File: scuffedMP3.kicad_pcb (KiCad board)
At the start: 2 copper layers, 24 x 16 mm, 10 parts, among them J1 OLED, J2 Micro_SD_Card, J3 AudioJack3, U1 ESP32-WROVER-E, U2 TP4056-42-ESOP8, U3 CP2102N-Axx-xQFN24, U4 MCP1825S, U5 PCM5102A

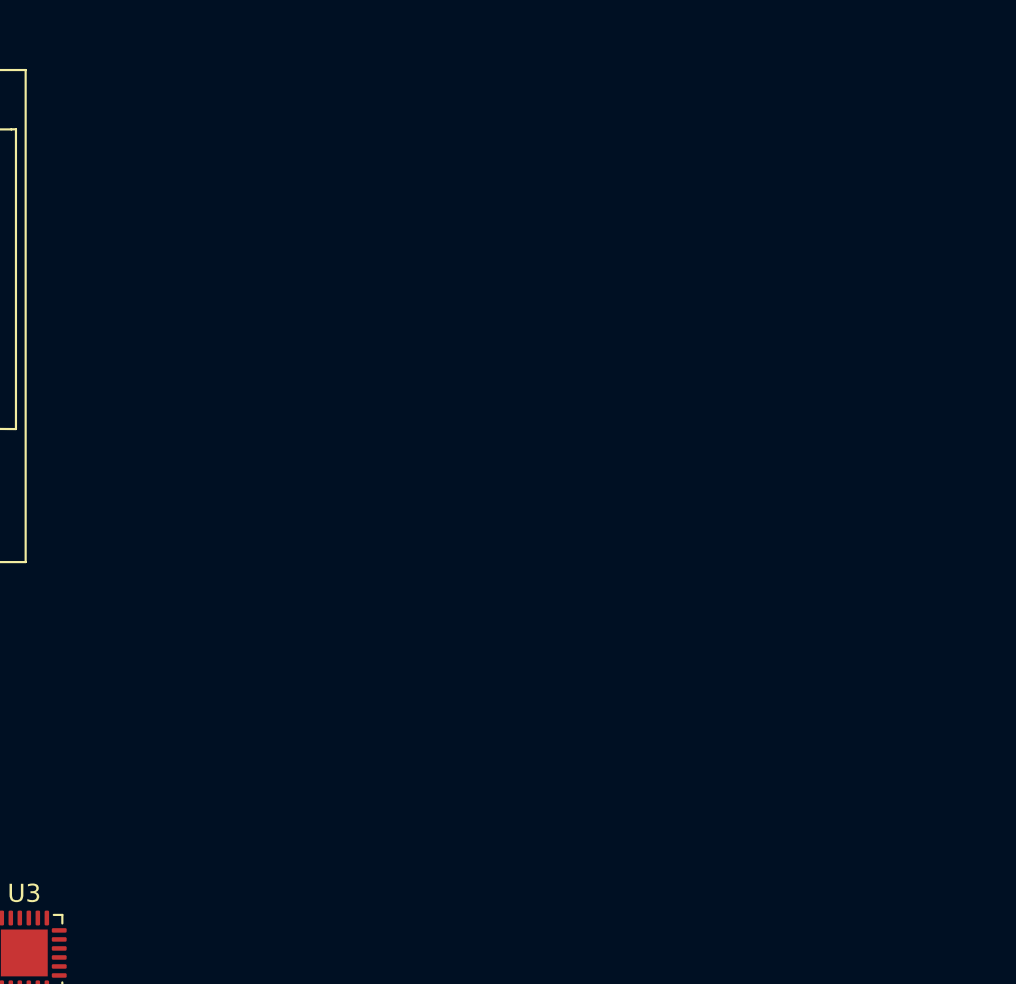
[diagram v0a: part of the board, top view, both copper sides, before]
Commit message: add touch sensor and wheel
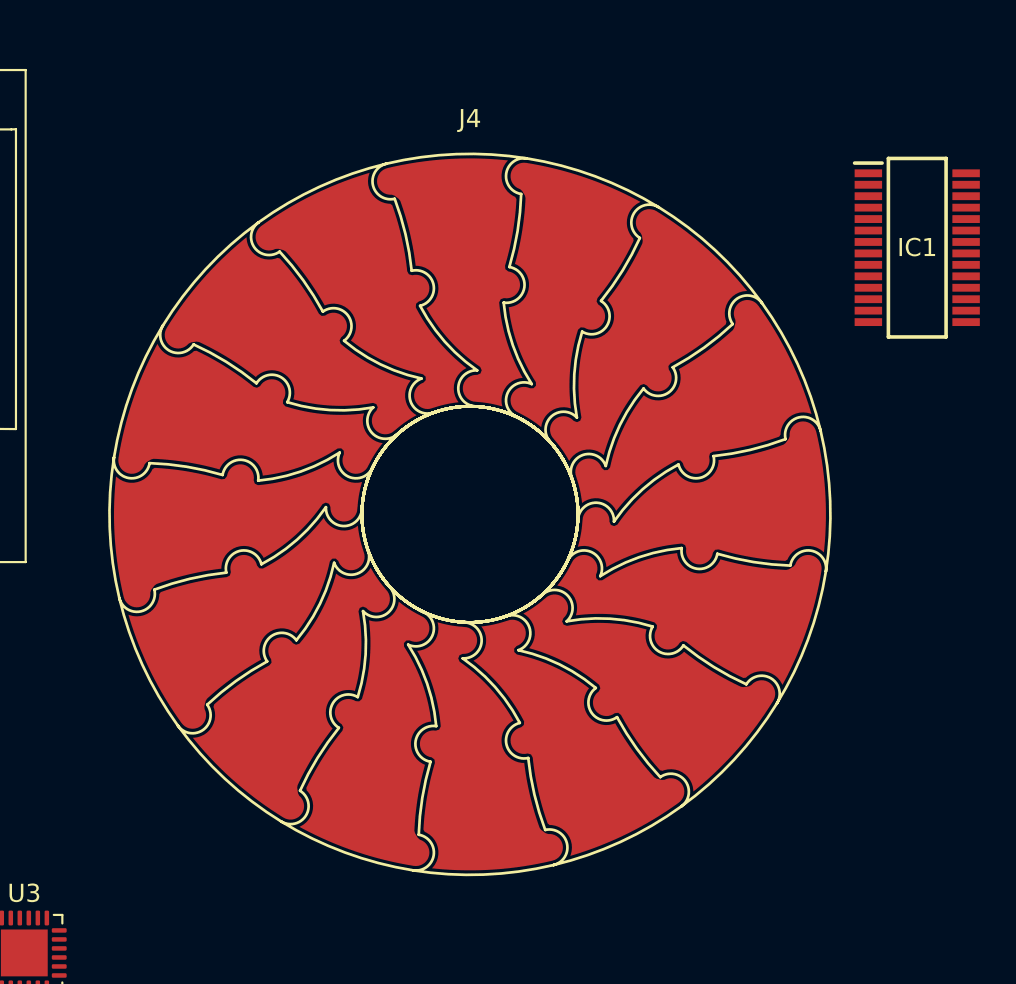
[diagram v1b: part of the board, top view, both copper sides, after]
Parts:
- added IC1: TTP229-BSF, TTP229-BSF:SOP64P600X175-28N, F.Cu at (131.3, 39.9)
- added J4: Conn_01x16_Pin, Library:ScrollWheel-40x12mm, F.Cu at (106.5, 54.7)
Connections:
- U1 pad 6: unconnected-(U1-GPIO34/ADC1_CH6-Pad6) -> Net-(IC1-SCL)
- U1 pad 7: unconnected-(U1-GPIO35/ADC1_CH7-Pad7) -> Net-(IC1-SDO)

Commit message: upd
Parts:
- removed BT1: Battery, Connector_JST:JST_PH_S2B-PH-K_1x02_P2.00mm_Horizontal
- added 10kΩ1: R, Resistor_SMD:R_0603_1608Metric, F.Cu at (108.4, 81.6)
- added C1: 1 µF, Capacitor_SMD:C_0603_1608Metric, F.Cu at (108.4, 84.1)
- added C10: 1 µF, Capacitor_SMD:C_0603_1608Metric, F.Cu at (112.4, 89.1)
- added C11: 0.1uF, Capacitor_SMD:C_0603_1608Metric, F.Cu at (112.4, 91.7)
- added C12: 0.1 µF, Capacitor_SMD:C_0603_1608Metric, F.Cu at (112.4, 94.2)
- added C13: 0.1 µF, Capacitor_SMD:C_0603_1608Metric, F.Cu at (112.4, 96.7)
- added C14: 1 µF, Capacitor_SMD:C_0603_1608Metric, F.Cu at (116.4, 81.6)
- added C15: 1 µF, Capacitor_SMD:C_0603_1608Metric, F.Cu at (116.4, 84.1)
- added C16: 1 µF, Capacitor_SMD:C_0603_1608Metric, F.Cu at (116.4, 86.6)
- added C17: 0.1 µF, Capacitor_SMD:C_0603_1608Metric, F.Cu at (116.4, 89.1)
- added C18: 0.1 µF, Capacitor_SMD:C_0603_1608Metric, F.Cu at (116.4, 91.7)
- added C2: 0.1 µF, Capacitor_SMD:C_0603_1608Metric, F.Cu at (108.4, 86.6)
- added C3: 1 µF, Capacitor_SMD:C_0603_1608Metric, F.Cu at (108.4, 89.1)
- added C4: 0.1 µF, Capacitor_SMD:C_0603_1608Metric, F.Cu at (108.4, 91.7)
- added C5: 0.1µF, Capacitor_SMD:C_0603_1608Metric, F.Cu at (108.4, 94.2)
- added C6: 0.1µF, Capacitor_SMD:C_0603_1608Metric, F.Cu at (108.4, 96.7)
- added C7: 0.1µF, Capacitor_SMD:C_0603_1608Metric, F.Cu at (112.4, 81.6)
- added C8: 1 µF, Capacitor_SMD:C_0603_1608Metric, F.Cu at (112.4, 84.1)
- added C9: 1 µF, Capacitor_SMD:C_0603_1608Metric, F.Cu at (112.4, 86.6)
- added R1: 10kΩ, Resistor_SMD:R_0603_1608Metric, F.Cu at (116.4, 94.2)
- added R2: 1.2 kΩ, Resistor_SMD:R_0603_1608Metric, F.Cu at (116.4, 96.7)
- added R3: 10 kΩ, Resistor_SMD:R_0603_1608Metric, F.Cu at (120.4, 81.6)
- added R4: 10 kΩ, Resistor_SMD:R_0603_1608Metric, F.Cu at (120.4, 84.1)
- added R5: 5.1 kΩ, Resistor_SMD:R_0603_1608Metric, F.Cu at (120.4, 86.6)
- added R6: 5.1 kΩ, Resistor_SMD:R_0603_1608Metric, F.Cu at (120.4, 89.1)
- added SW1: SW_SPST, Button_Switch_SMD:SW_DIP_SPSTx01_Slide_6.7x4.1mm_W6.73mm_P2.54mm_LowProfile_JPin, F.Cu at (165.2, 113.4)
- added U6: HS24S010B, OLED:LCD-TH_L72.3-W43.0_HS24S010B, F.Cu at (199.2, 40.3)
- J1: value OLED -> battery; footprint OLED:128x64OLED -> PHR-2:JST_PHR-2
- J2: value Micro_SD_Card -> DM3AT-SF-PEJM5; footprint Connector_Card:SD_Card_Device_16mm_SlotDepth -> micro_sd:HRS_DM3AT-SF-PEJM5
- J4: footprint Library:ScrollWheel-40x12mm -> Wheel:ScrollWheel-60x35mm
- moved U5 190.8 mm to (223.1, 123.9)
- moved J3 184.6 mm to (231.8, 129.5), turned to 90 degrees
- moved J2 164.2 mm to (230.9, 70.0), turned to 90 degrees
- moved U1 163.7 mm to (199.8, 94.3)
- moved J1 142.9 mm to (187.0, 121.3), turned to 90 degrees
- moved U4 140.0 mm to (176.1, 125.0)
- moved USB1 138.1 mm to (165.3, 128.6)
- moved J4 101.4 mm to (198.9, 96.5)
- moved U3 99.3 mm to (173.0, 118.0)
- moved U2 93.8 mm to (164.6, 105.1)
- moved IC1 48.8 mm to (167.7, 72.3)
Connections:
- net Net-(IC1-TP0) renamed /TOUCH TP0
- net Net-(IC1-TP1) renamed /TOUCH TP1
- net Net-(IC1-TP2) renamed /TOUCH TP2
- net Net-(IC1-TP3) renamed /TOUCH TP3
- net Net-(IC1-TP4) renamed /TOUCH TP4
- IC1 pad 10: Net-(IC1-TP13) -> /TOUCH TP13
- IC1 pad 11: Net-(IC1-TP12) -> /TOUCH TP12
- IC1 pad 12: Net-(IC1-SDO) -> /TOUCH SDO
- IC1 pad 13: Net-(IC1-SCL) -> /TOUCH SCL
- IC1 pad 14: unconnected-(IC1-SLPSENB-Pad14) -> GND
- IC1 pad 15: Net-(IC1-TP11) -> /TOUCH TP11
- IC1 pad 16: Net-(IC1-TP10) -> /TOUCH TP10
- IC1 pad 17: unconnected-(IC1-SENADJ2-Pad17) -> GND
- IC1 pad 18: Net-(IC1-TP9) -> /TOUCH TP9
- IC1 pad 19: Net-(IC1-TP8) -> /TOUCH TP8
- IC1 pad 20: unconnected-(IC1-TEST-Pad20) -> GND
- IC1 pad 21: Net-(IC1-TP7) -> /TOUCH TP7
- IC1 pad 22: Net-(IC1-TP6) -> /TOUCH TP6
- IC1 pad 23: unconnected-(IC1-SENADJ1-Pad23) -> GND
- IC1 pad 24: Net-(IC1-TP5) -> /TOUCH TP5
- IC1 pad 26: Net-(IC1-VDD) -> +3V3
- IC1 pad 27: Net-(BT1--) -> GND
- IC1 pad 28: unconnected-(IC1-SLPSENA-Pad28) -> Net-(IC1-SLPSENA)
- IC1 pad 4: unconnected-(IC1-SENADJ0-Pad4) -> GND
- IC1 pad 7: Net-(IC1-TP15) -> /TOUCH TP15
- IC1 pad 8: Net-(IC1-TP14) -> /TOUCH TP14
- IC1 pad 9: unconnected-(IC1-SENADJ3-Pad9) -> +3V3
- J1 pad 1: Net-(J1-Pin_1) -> /BAT
- J1 pad 2: Net-(J1-Pin_2) -> GND
- J2 pad 2: Net-(J2-DAT3/CD) -> /MICRO CD
- J2 pad 3: Net-(J2-CMD) -> /MICRO CMD
- J2 pad 4: Net-(IC1-VDD) -> +3V3
- J2 pad 5: Net-(J2-CLK) -> /MICRO CLK
- J2 pad 6: Net-(BT1--) -> GND
- J2 pad 7: Net-(J2-DAT0) -> /MICRO DAT0
- J3 pad S: Net-(BT1--) -> GND
- U1 pad 1: Net-(BT1--) -> GND
- U1 pad 10: Net-(U1-DAC_1/ADC2_CH8/GPIO25) -> /LR CLOCK
- U1 pad 11: Net-(U1-DAC_2/ADC2_CH9/GPIO26) -> /Bit Clock
- U1 pad 12: Net-(U1-ADC2_CH7/GPIO27) -> /OLED DC
- U1 pad 15: Net-(BT1--) -> GND
- U1 pad 2: Net-(IC1-VDD) -> +3V3
- U1 pad 24: unconnected-(U1-ADC2_CH2/GPIO2-Pad24) -> /MICRO CLK
- U1 pad 25: unconnected-(U1-GPIO0/BOOT/ADC2_CH1-Pad25) -> /BOOT_SEL
- U1 pad 26: unconnected-(U1-ADC2_CH0/GPIO4-Pad26) -> /MICRO CMD
- U1 pad 29: Net-(J2-DAT3/CD) -> /OLED CS
- U1 pad 3: unconnected-(U1-EN/CHIP_PU-Pad3) -> /EN
- U1 pad 30: Net-(J2-CLK) -> /OLED SCL
- U1 pad 31: Net-(J2-DAT0) -> /OLED RST
- U1 pad 33: Net-(J1-Pin_1) -> /OLED LED
- U1 pad 34: Net-(U1-U0RXD/GPIO3) -> /UART_RXD
- U1 pad 35: Net-(U1-U0TXD/GPIO1) -> /UART_TXD
- U1 pad 36: Net-(J1-Pin_2) -> /DAC DIN
- U1 pad 37: Net-(J2-CMD) -> /MOSI OLED
- U1 pad 38: Net-(BT1--) -> GND
- U1 pad 6: Net-(IC1-SCL) -> unconnected-(U1-GPIO34/ADC1_CH6-Pad6)
- U1 pad 7: Net-(IC1-SDO) -> unconnected-(U1-GPIO35/ADC1_CH7-Pad7)
- U1 pad 8: unconnected-(U1-32K_XP/GPIO32/ADC1_CH4-Pad8) -> /MICRO DAT0
- U1 pad 9: unconnected-(U1-32K_XN/GPIO33/ADC1_CH5-Pad9) -> /TOUCH SCL
- U2 pad 2: unconnected-(U2-PROG-Pad2) -> Net-(U2-PROG)
- U2 pad 3: Net-(BT1--) -> GND
- U2 pad 4: Net-(U2-V_{CC}) -> VBUS
- U2 pad 5: Net-(BT1-+) -> /BAT
- U2 pad 8: Net-(BT1--) -> VBUS
- U3 pad 19: unconnected-(U3-~{RTS}-Pad19) -> Net-(U3-~{RTS})
- U3 pad 2: Net-(BT1--) -> GND
- U3 pad 20: Net-(U1-U0TXD/GPIO1) -> /UART_RXD
- U3 pad 21: Net-(U1-U0RXD/GPIO3) -> /UART_TXD
- U3 pad 23: unconnected-(U3-~{DTR}-Pad23) -> Net-(U3-~{DTR})
- U3 pad 25: Net-(BT1--) -> GND
- U3 pad 3: unconnected-(U3-D+-Pad3) -> /USB_DP
- U3 pad 4: unconnected-(U3-D--Pad4) -> /USB_DM
- U3 pad 6: unconnected-(U3-VDD-Pad6) -> +3V3
- U3 pad 7: unconnected-(U3-VREGIN-Pad7) -> VBUS
- U3 pad 8: unconnected-(U3-VBUS-Pad8) -> VBUS
- U3 pad 9: unconnected-(U3-~{RST}-Pad9) -> Net-(U3-~{RST})
- U4 pad 1: Net-(BT1-+) -> VBUS
- U4 pad 2: Net-(BT1--) -> GND
- U4 pad 3: Net-(IC1-VDD) -> /3V3 IN
- U5 pad 1: Net-(IC1-VDD) -> +3V3
- U5 pad 10: Net-(BT1--) -> unconnected-(U5-DEMP-Pad10)
- U5 pad 11: Net-(BT1--) -> unconnected-(U5-FLT-Pad11)
- U5 pad 13: Net-(U1-ADC2_CH7/GPIO27) -> /Bit Clock
- U5 pad 14: Net-(U1-DAC_1/ADC2_CH8/GPIO25) -> /DAC DIN
- U5 pad 15: Net-(U1-DAC_2/ADC2_CH9/GPIO26) -> /LR CLOCK
- U5 pad 16: Net-(BT1--) -> GND
- U5 pad 17: Net-(IC1-VDD) -> GND
- U5 pad 19: Net-(BT1--) -> GND
- U5 pad 2: unconnected-(U5-CAPP-Pad2) -> Net-(U5-CAPP)
- U5 pad 20: Net-(IC1-VDD) -> +3V3
- U5 pad 3: Net-(BT1--) -> GND
- U5 pad 4: unconnected-(U5-CAPM-Pad4) -> Net-(U5-CAPM)
- U5 pad 5: Net-(BT1--) -> Net-(U5-VNEG)
- U5 pad 8: Net-(IC1-VDD) -> +3V3
- U5 pad 9: Net-(BT1--) -> GND
- USB1 pad 1: unconnected-(USB1-GND-Pad1) -> GND
- USB1 pad 12: unconnected-(USB1-GND-Pad12) -> GND
- USB1 pad 13: unconnected-(USB1-GND-Pad13) -> GND
- USB1 pad 16: unconnected-(USB1-VBUS-Pad16) -> VBUS
- USB1 pad 17: unconnected-(USB1-CC2-Pad17) -> Net-(USB1-CC2)
- USB1 pad 21: unconnected-(USB1-VBUS-Pad21) -> VBUS
- USB1 pad 24: Net-(BT1--) -> GND
- USB1 pad 25: unconnected-(USB1-Center_Plate_Pin-Pad25) -> GND
- USB1 pad 26: Net-(BT1--) -> GND
- USB1 pad 27: unconnected-(USB1-Under-Barrel_Pads-Pad27) -> GND
- USB1 pad 4: unconnected-(USB1-VBUS-Pad4) -> VBUS
- USB1 pad 5: unconnected-(USB1-CC1-Pad5) -> Net-(USB1-CC1)
- USB1 pad 6: Net-(U1-U0RXD/GPIO3) -> unconnected-(USB1-Dp1-Pad6)
- USB1 pad 7: Net-(U1-U0TXD/GPIO1) -> unconnected-(USB1-Dn1-Pad7)
- USB1 pad 9: Net-(U2-V_{CC}) -> VBUS
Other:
- board size 24 x 16 mm -> 79.9 x 114.6 mm
